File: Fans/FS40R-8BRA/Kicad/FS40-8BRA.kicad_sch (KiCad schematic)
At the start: 65 parts, among them SW1 TIMER, SW2 TIMER, SW3 TIMER, SW4 TIMER, T1 Z0607, T2 Z0607, T3 Z0607, T4 Z0607, U1 SN8P2602BP

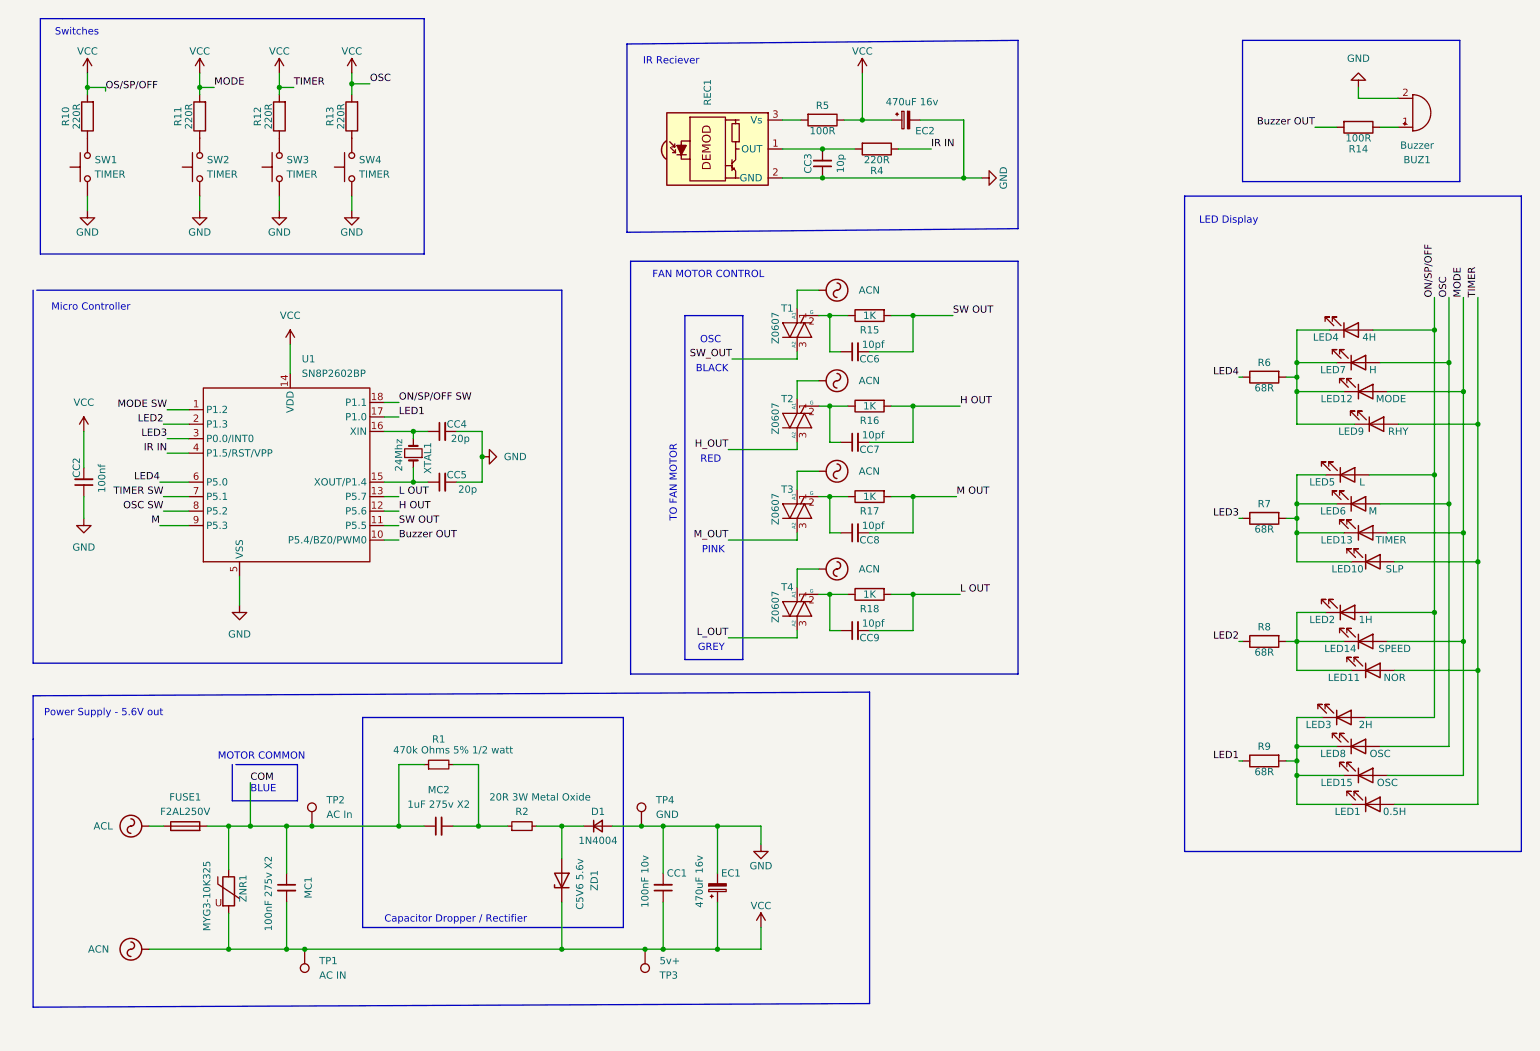
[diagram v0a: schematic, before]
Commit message: added mod to FS40R
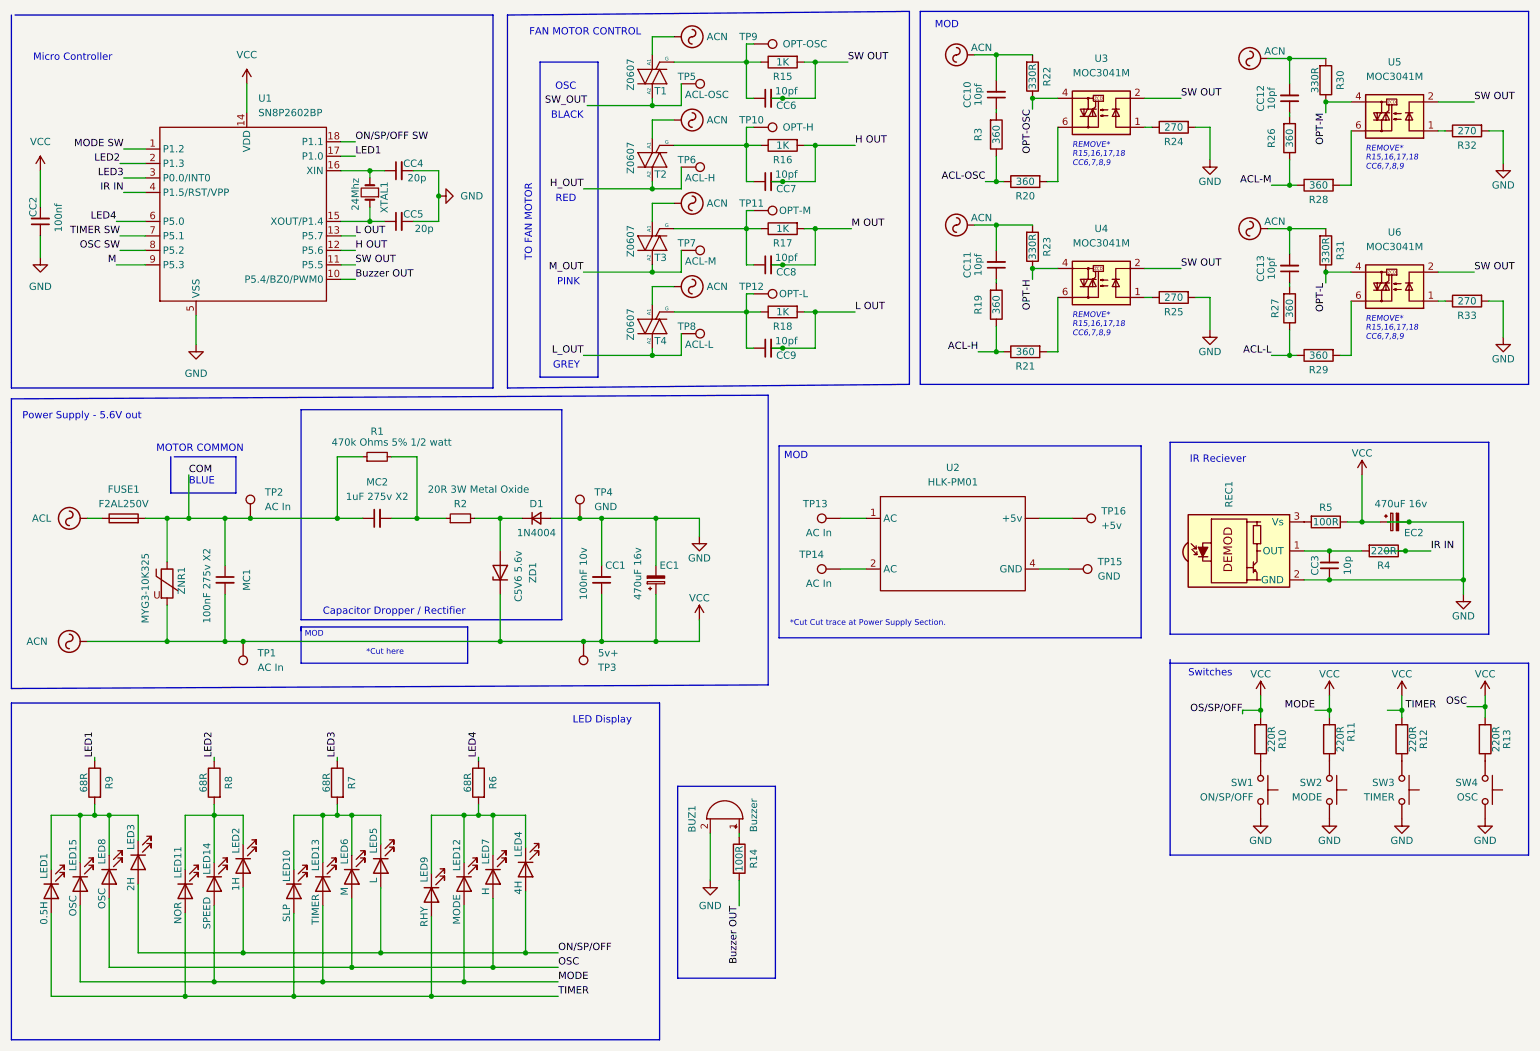
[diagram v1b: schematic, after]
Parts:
- added CC10, CC11, CC12, CC13: 10pf, symbol Device:C_Small
- added R19, R20, R21, R26, R27, R28, R29, R3: 360, symbol Device:R
- added R22, R23, R30, R31: 330R, symbol Device:R
- added R24, R25, R32, R33: 270, symbol Device:R
- added TP10: OPT-H, symbol Connector:TestPoint
- added TP11: OPT-M, symbol Connector:TestPoint
- added TP12: OPT-L, symbol Connector:TestPoint
- added TP13, TP14: AC In, symbol Connector:TestPoint
- added TP15: GND, symbol Connector:TestPoint
- added TP16: +5v, symbol Connector:TestPoint
- added TP5: ACL-OSC, symbol Connector:TestPoint
- added TP6: ACL-H, symbol Connector:TestPoint
- added TP7: ACL-M, symbol Connector:TestPoint
- added TP8: ACL-L, symbol Connector:TestPoint
- added TP9: OPT-OSC, symbol Connector:TestPoint
- added U2: HLK-PM01, symbol terence:HLK-PM01
- added U3, U4, U5, U6: MOC3041M, symbol Relay_SolidState:MOC3041M
- SW1: value TIMER -> ON/SP/OFF
- SW2: value TIMER -> MODE
- SW4: value TIMER -> OSC
- TP1: value AC IN -> AC In
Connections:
- net AC: now also CC10.2, CC11.2, CC12.2, CC13.2, R22.2, R23.2, R30.2, R31.2; no longer LED1.2 (A), LED10.2 (A), LED11.2 (A), LED9.2 (A)
- net GND: now also R24.2, R25.2, R32.2, R33.2
- net H_OUT: now also TP6.1
- net L_OUT: now also TP8.1
- net M_OUT: now also TP7.1
- net SW OUT: now also U3.2, U4.2, U5.2, U6.2
- net SW_OUT: now also TP5.1
- net at CC8.1, R17.1, T3.2 (G): now also TP11.1
- net at CC7.1, R16.1, T2.2 (G): now also TP10.1
- net at CC9.1, R18.1, T4.2 (G): now also TP12.1
- net at CC6.1, R15.1, T1.2 (G): now also TP9.1
- new net: TP13.1, U2.1 (AC)
- new net: CC13.1, R27.2
- new net: CC11.1, R19.2
- new net: R33.1, U6.1
- new net: R29.2, U6.6
- new net: TP16.1, U2. (+5v)
- new net: TP14.1, U2.2 (AC)
- new net: TP15.1, U2.4 (GND)
- new net: CC12.1, R26.2
- new net: R32.1, U5.1
- new net: R28.2, U5.6
- new net: CC10.1, R3.2
- new net: R20.2, U3.6
- new net: R25.1, U4.1
- new net: R21.2, U4.6
- new net: R24.1, U3.1
- new net ACL-H: R19.1, R21.1
- new net ACL-L: R27.1, R29.1
- new net ACL-M: R26.1, R28.1
- new net ACL-OSC: R20.1, R3.1
- new net OPT-H: R23.1, U4.4
- new net OPT-L: R31.1, U6.4
- new net OPT-M: R30.1, U5.4
- new net OPT-OSC: R22.1, U3.4
- new net TIMER: LED1.2 (A), LED10.2 (A), LED11.2 (A), LED9.2 (A)
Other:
- note added: "*Cut Cut trace at Power Supply Section."
- note added: "*Cut here"
- note added: "MOD"
- note added: "R15,16,17,18 CC6,7,8,9"
- note added: "REMOVE*"
- moved on the sheet: BUZ1, CC1, CC2, CC3, CC4, CC5, CC6, CC7, CC8, CC9, D1, EC1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
